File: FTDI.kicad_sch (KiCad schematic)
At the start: 23 parts, among them U5 FT4232H_VQFN, Y1 Resonator_12MHz_ABM8G

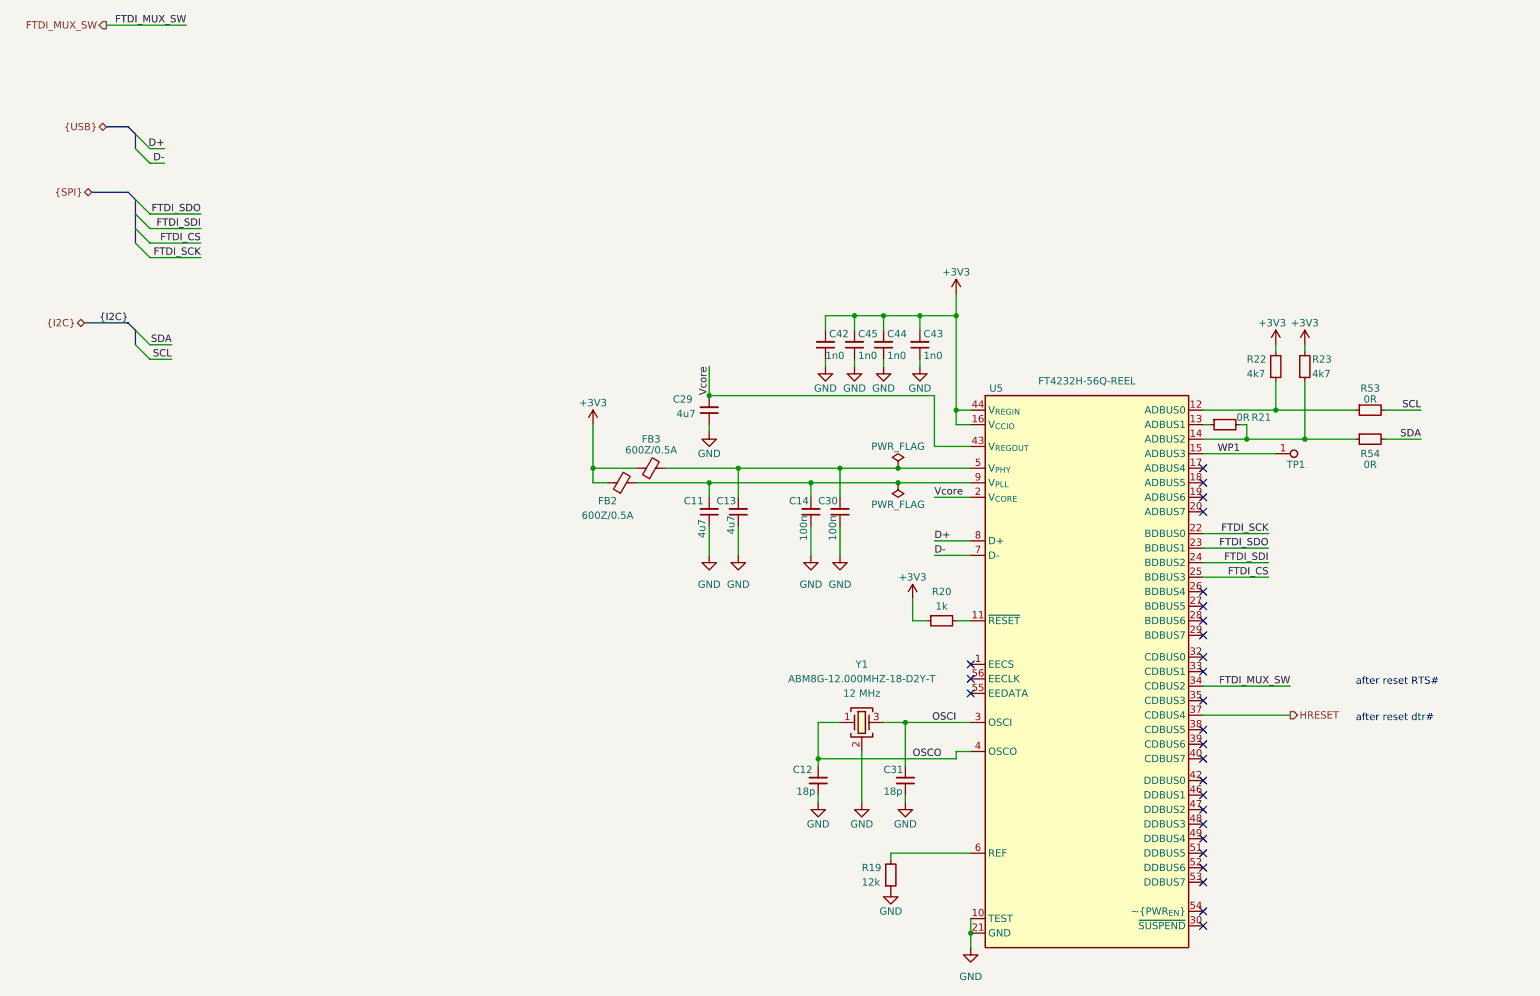
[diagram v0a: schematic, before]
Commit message: [#66725] Implement changes from review for rev 1.1.0
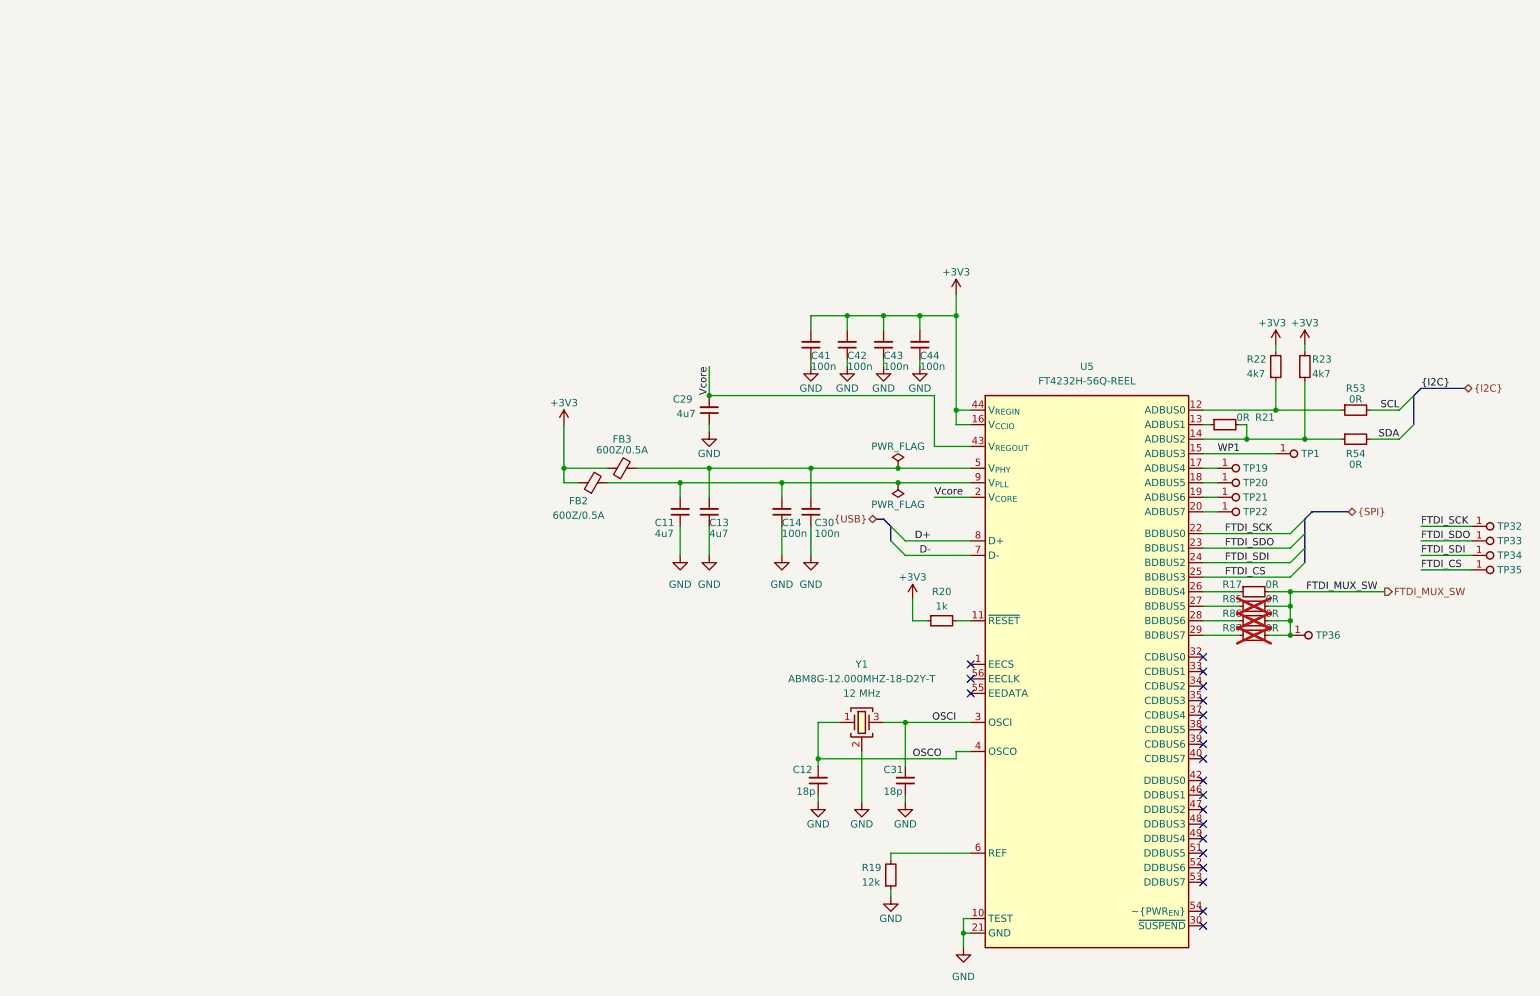
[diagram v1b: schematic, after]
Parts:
- removed C14, C30: C_100n_16V_X7R_0402, antmicro-footprints:C_0402_1005Metric, symbol antmicroCapacitors0402:C_100n_16V_X7R_0402
- removed C42, C43, C44, C45: C_1n0_0402, antmicro-footprints:C_0402_1005Metric, symbol antmicroCapacitors0402:C_1n0_0402
- removed TP1: TP_1.5mm_SMD, antmicro-footprints:TP_SMD_1.5mm, symbol antmicroTestPoints:TP_1.5mm_SMD
- added C14, C30, C41, C42, C43, C44: C_100n_0402, antmicro-footprints:C_0402_1005Metric, symbol antmicroCapacitors0402:C_100n_0402
- added R17, R85, R86, R87: R_0R_0402, antmicro-footprints:R_0402_1005Metric, symbol antmicroResistors0402:R_0R_0402
- added TP1, TP19, TP20, TP21, TP22, TP32, TP33, TP34, TP35, TP36: TP_0.75mm_SMD, antmicro-footprints:TP_SMD_0.75mm, symbol antmicroTestPoints:TP_0.75mm_SMD
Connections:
- net +3V3: now also C41.2, C42.2, C43.2, C44.2
- net FTDI_CS: now also TP35.1
- net FTDI_MUX_SW: now also R17.2, R85.2, R86.2, R87.2, TP36.1; no longer U5.34 (CDBUS2)
- net FTDI_SCK: now also TP32.1
- net FTDI_SDI: now also TP34.1
- net FTDI_SDO: now also TP33.1
- net GND: now also C14.1, C30.1, C41.1, C42.1, C43.1, C44.1
- net WP1: now also TP1.1
- net at C13.2, FB3.2, U5.5 (V_{PHY}): now also C30.2
- net at C11.2, FB2.2, U5.9 (V_{PLL}): now also C14.2
- net at U5.17 (ADBUS4): now also TP19.1
- net at U5.18 (ADBUS5): now also TP20.1
- net at U5.19 (ADBUS6): now also TP21.1
- net at U5.20 (ADBUS7): now also TP22.1
- net at U5.26 (BDBUS4): now also R17.1
- net at U5.27 (BDBUS5): now also R85.1
- net at U5.28 (BDBUS6): now also R86.1
- net at U5.29 (BDBUS7): now also R87.1
- net HRESET: no longer names the net of U5.37 (CDBUS4)
- no-connect marks 27 -> 21
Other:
- note removed: "after reset RTS#"
- note removed: "after reset dtr#"
- moved on the sheet: C11, C13, FB2, FB3, R53, R54
